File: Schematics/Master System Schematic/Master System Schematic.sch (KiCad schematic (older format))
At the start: 30 parts, among them J1 GND, J2 TS+, J3 TS-, SW1 GLVMS, SW2 SideMounted (BRB), SW3 SideMounted (BRB)

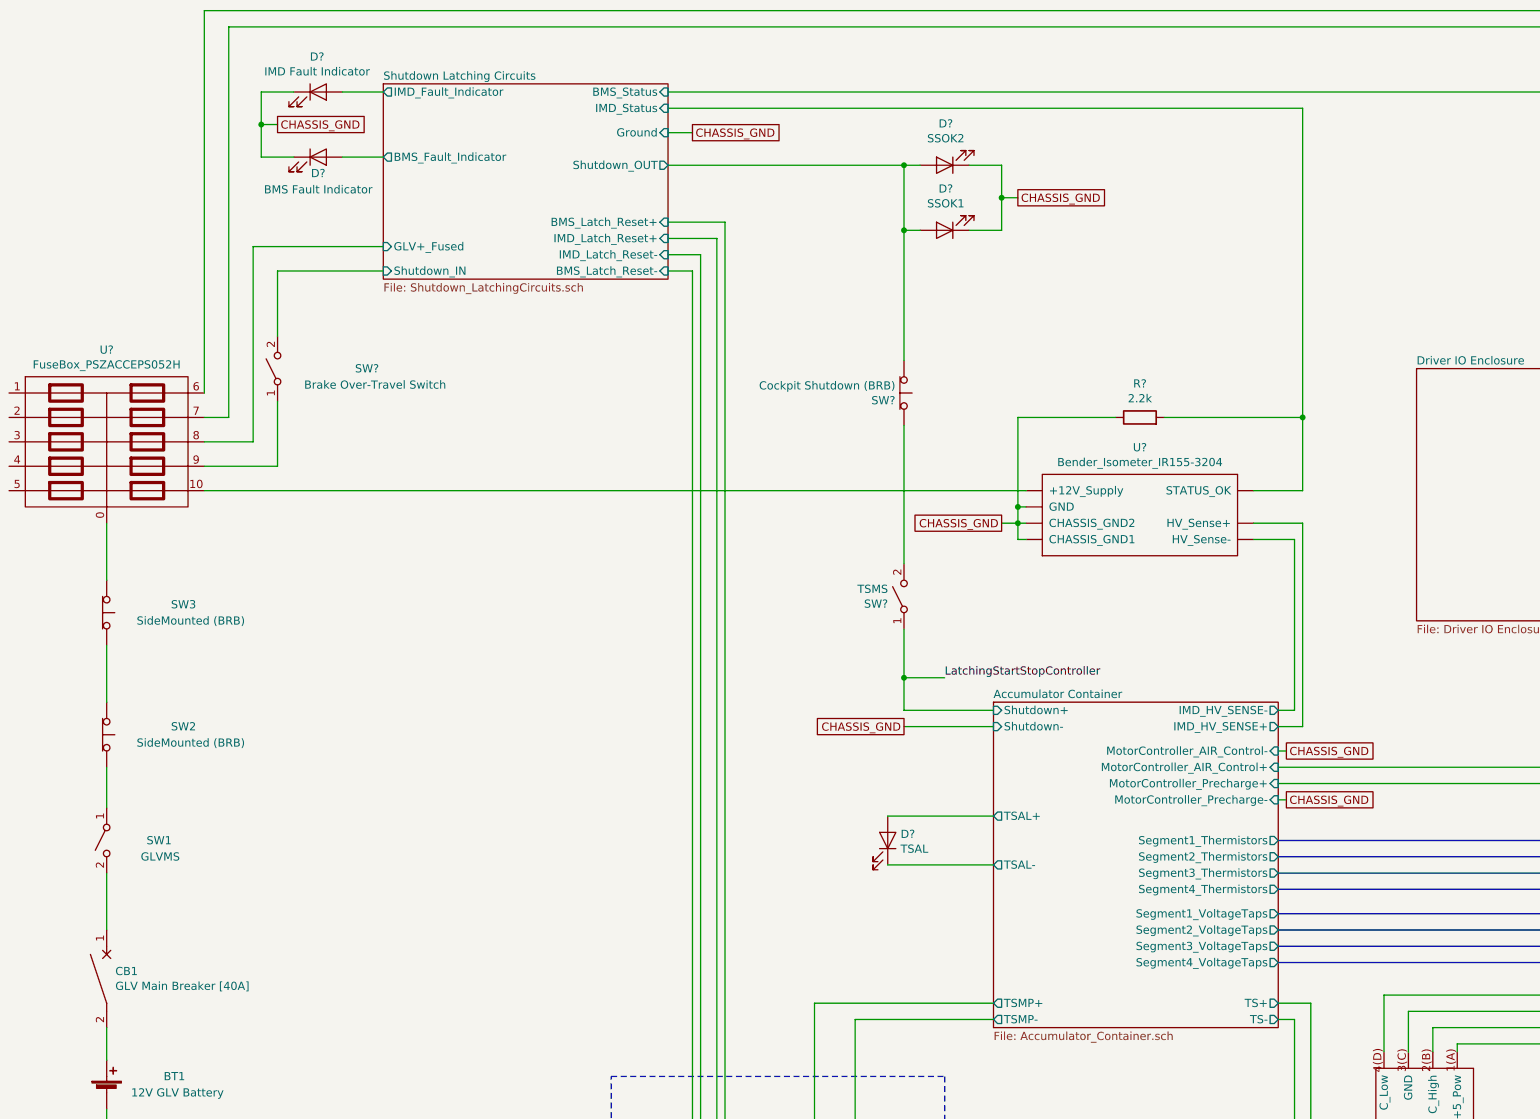
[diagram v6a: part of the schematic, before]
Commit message: Wire run updates, prettying up
>Moved SMDs and HVDs outside of accumulator container for consistency (all human activated switches and indicators should be in top level sheet)
>minor wire run updates and cleanup in accumulator container
>minor wire run cleanup in master schematic
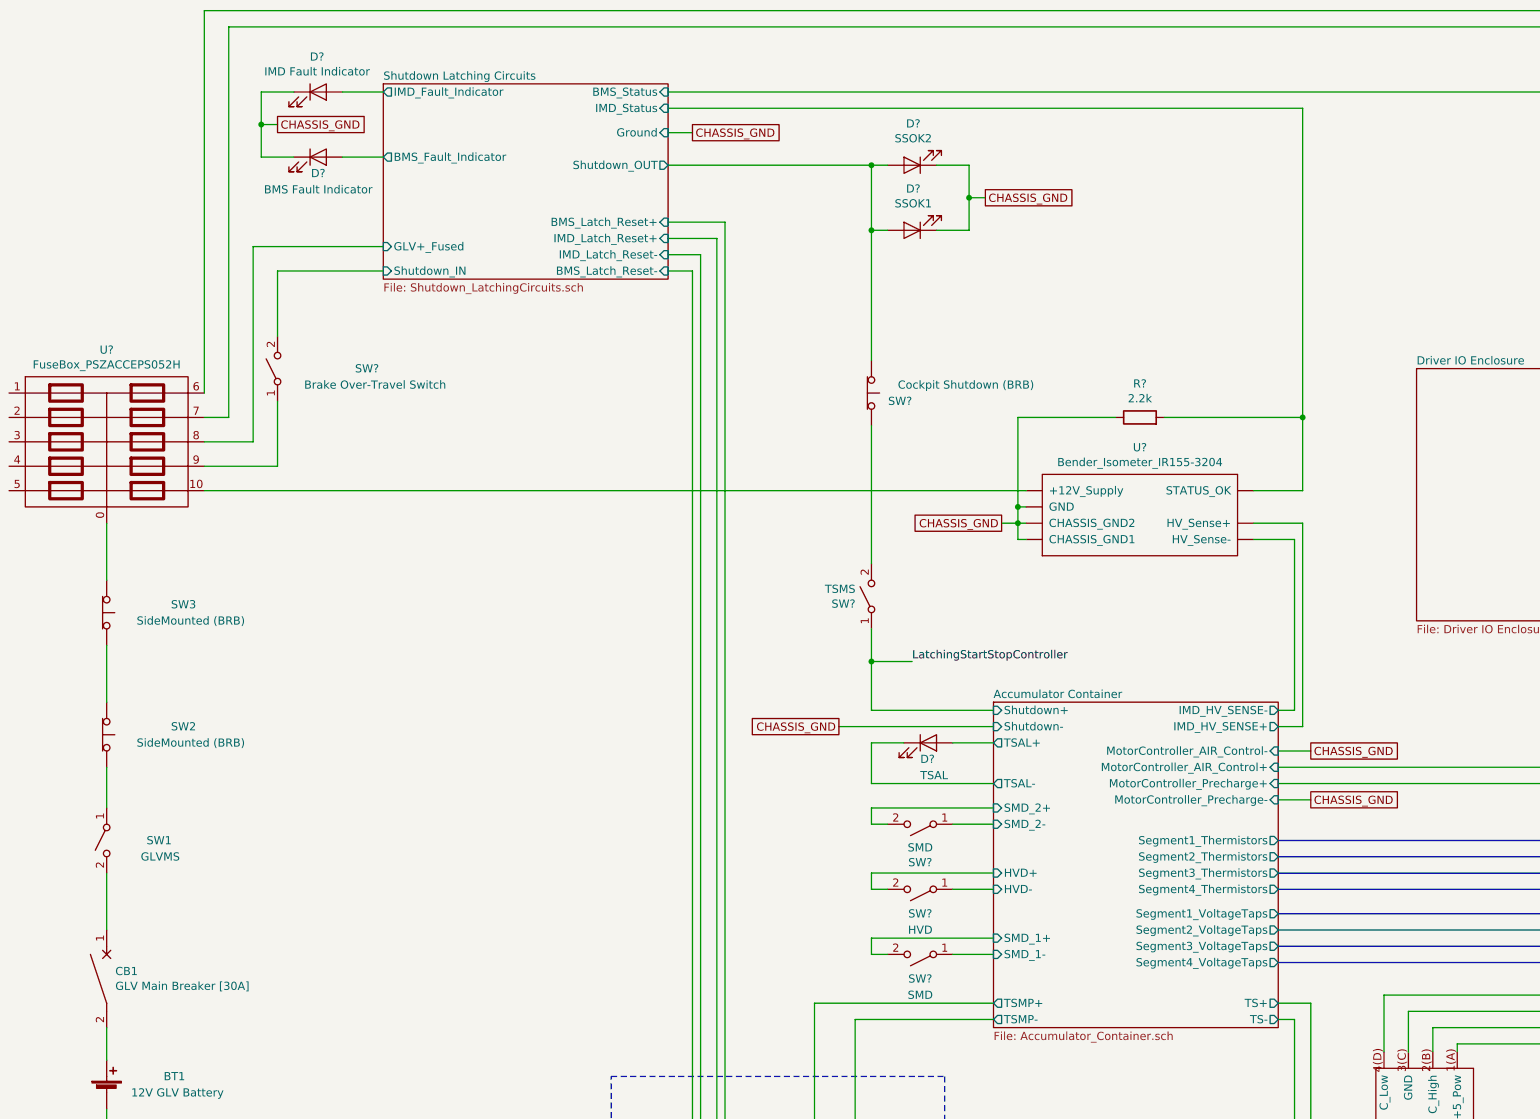
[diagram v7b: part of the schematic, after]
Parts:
- added SW?: HVD, symbol Switch:SW_SPST
- added SW? (x2): SMD, symbol Switch:SW_SPST
- CB1: value GLV Main Breaker [40A] -> GLV Main Breaker [30A]
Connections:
- new net: U?.23 (CANB_H), U?.6, U?.8 (Reverse_Enable_Switch)
- new net: U?.~ (AC3), U?.~ (TS-) (x2)
- new net Accumulator Container/HVD+: SW?.2 (B)
- new net Accumulator Container/HVD-: SW?.1 (A)
- new net Accumulator Container/SMD_1+: SW?.2 (B)
- new net Accumulator Container/SMD_1-: SW?.1 (A)
- new net Accumulator Container/SMD_2+: SW?.2 (B)
- new net Accumulator Container/SMD_2-: SW?.1 (A)
- now unconnected: U?.23 (CANB_H), U?.8 (Reverse_Enable_Switch)
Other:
- moved on the sheet: D?, SW?
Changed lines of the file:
@@
 L Switch:SW_Push_Open SW?
 U 1 1 5F67997D
-P 6150 3350
+P 5950 3350
 AR Path="/5F45AFB3/5F67997D" Ref="SW?"  Part="1"
 AR Path="/5F67997D" Ref="SW?"  Part="1"
-F 0 "SW?" V 6196 3297 50  0000 R CNN
-F 1 "Cockpit Shutdown (BRB)" V 6105 3297 50  0000 R CNN
-F 2 "" H 6150 3550 50  0001 C CNN
-F 3 "https://www.mouser.com/datasheet/2/307/a165e_ds_e_11_2_csm1264-1291086.pdf" H 6150 3550 50  0001 C CNN
-	1    6150 3350
+F 0 "SW?" V 6000 3600 50  0000 R CNN
+F 1 "Cockpit Shutdown (BRB)" V 5900 4350 50  0000 R CNN
+F 2 "" H 5950 3550 50  0001 C CNN
+F 3 "https://www.mouser.com/datasheet/2/307/a165e_ds_e_11_2_csm1264-1291086.pdf" H 5950 3550 50  0001 C CNN
+	1    5950 3350
 	0    1    1    0
 $EndComp
@@
 L Switch:SW_SPST SW?
 U 1 1 5F67998A
-P 6150 4600
+P 5950 4600
 AR Path="/5F45AFB3/5F67998A" Ref="SW?"  Part="1"
 AR Path="/5F67998A" Ref="SW?"  Part="1"
-F 0 "SW?" V 6104 4698 50  0000 L CNN
-F 1 "TSMS" V 6195 4698 50  0000 L CNN
-F 2 "" H 6150 4600 50  0001 C CNN
-F 3 "https://www.pegasusautoracing.com/pdfs/4430WiringInstructions.pdf" H 6150 4600 50  0001 C CNN
-	1    6150 4600
+F 0 "SW?" V 5904 4698 50  0000 L CNN
+F 1 "TSMS" V 5995 4698 50  0000 L CNN
+F 2 "" H 5950 4600 50  0001 C CNN
+F 3 "https://www.pegasusautoracing.com/pdfs/4430WiringInstructions.pdf" H 5950 4600 50  0001 C CNN
+	1    5950 4600
 	0    -1   -1   0
 $EndComp
 Text GLabel 1400 7900 2    50   UnSpc ~ 0
 CHASSIS_GND
-Text Label 6400 5100 0    50   ~ 0
+Text Label 6200 5000 0    50   ~ 0
 LatchingStartStopController
-Text GLabel 6850 2150 2    50   UnSpc ~ 0
-CHASSIS_GND
-Wire Wire Line
-	6750 2350 6750 2150
-Wire Wire Line
-	6550 1950 6750 1950
+Text GLabel 6650 2150 2    50   UnSpc ~ 0
+CHASSIS_GND
+Wire Wire Line
+	6550 2350 6550 2150
+Wire Wire Line
+	6350 1950 6550 1950
 $Comp
 L Device:LED D?
 U 1 1 5F67996F
-P 6400 2350
+P 6200 2350
 AR Path="/5F45AFB3/5F67996F" Ref="D?"  Part="1"
 AR Path="/5F67996F" Ref="D?"  Part="1"
-F 0 "D?" H 6393 2095 50  0000 C CNN
-F 1 "SSOK1" H 6393 2186 50  0000 C CNN
-F 2 "" H 6400 2350 50  0001 C CNN
-F 3 "https://www.superbrightleds.com/moreinfo/marker-clearance/rectangle-led-truck-and-trailer-lights-4-double-bullseye-led-side-clearance-lights-w-12-high-flux-leds-pigtail-connector/596/" H 6400 2350 50  0001 C CNN
-	1    6400 2350
+F 0 "D?" H 6193 2095 50  0000 C CNN
+F 1 "SSOK1" H 6193 2186 50  0000 C CNN
+F 2 "" H 6200 2350 50  0001 C CNN
+F 3 "https://www.superbrightleds.com/moreinfo/marker-clearance/rectangle-led-truck-and-trailer-lights-4-double-bullseye-led-side-clearance-lights-w-12-high-flux-leds-pigtail-connector/596/" H 6200 2350 50  0001 C CNN
+	1    6200 2350
 	-1   0    0    1
 $EndComp
@@
 L Device:LED D?
 U 1 1 5F679969
-P 6400 1950
+P 6200 1950
 AR Path="/5F45AFB3/5F679969" Ref="D?"  Part="1"
 AR Path="/5F679969" Ref="D?"  Part="1"
-F 0 "D?" H 6393 1695 50  0000 C CNN
-F 1 "SSOK2" H 6393 1786 50  0000 C CNN
-F 2 "" H 6400 1950 50  0001 C CNN
-F 3 "https://www.superbrightleds.com/moreinfo/marker-clearance/rectangle-led-truck-and-trailer-lights-4-double-bullseye-led-side-clearance-lights-w-12-high-flux-leds-pigtail-connector/596/" H 6400 1950 50  0001 C CNN
-	1    6400 1950
+F 0 "D?" H 6193 1695 50  0000 C CNN
+F 1 "SSOK2" H 6193 1786 50  0000 C CNN
+F 2 "" H 6200 1950 50  0001 C CNN
+F 3 "https://www.superbrightleds.com/moreinfo/marker-clearance/rectangle-led-truck-and-trailer-lights-4-double-bullseye-led-side-clearance-lights-w-12-high-flux-leds-pigtail-connector/596/" H 6200 1950 50  0001 C CNN
+	1    6200 1950
 	-1   0    0    1
 $EndComp
@@
 	1400 7900 1250 7900
 Wire Wire Line
-	6850 2150 6750 2150
-Connection ~ 6750 2150
-Wire Wire Line
-	6750 2150 6750 1950
+	6650 2150 6550 2150
+Connection ~ 6550 2150
+Wire Wire Line
+	6550 2150 6550 1950
 $Comp
 L Device:R R?
@@
 	1250 7750 1250 7900
 Wire Wire Line
-	6750 2350 6550 2350
+	6550 2350 6350 2350
 Wire Wire Line
 	1250 7250 1250 7450
@@
 	1250 4900 1250 5250
 Wire Wire Line
-	6400 5100 6150 5100
+	6200 5000 5950 5000
 $Comp
 L Connector:Conn_01x01_Female J3
@@
 Text Notes 4400 8900 0    50   ~ 0
 TSMP and Shutdown Reset Container
-Text GLabel 6150 5400 0    50   UnSpc ~ 0
+Text GLabel 5750 5400 0    50   UnSpc ~ 0
 CHASSIS_GND
 $Comp
@@
 F5 "TS-" O L 8850 9050 50
 $EndSheet
-Text GLabel 8500 5850 2    50   UnSpc ~ 0
+Text GLabel 8650 5850 2    50   UnSpc ~ 0
 CHASSIS_GND
 $Sheet
@@
 F4 "TS+" O R 8450 7100 50
 F5 "TS-" O R 8450 7200 50
-F6 "TSAL+" O L 6700 5950 50
-F7 "TSAL-" O L 6700 6250 50
+F6 "TSAL+" O L 6700 5500 50
+F7 "TSAL-" O L 6700 5750 50
 F8 "IMD_HV_SENSE-" O R 8450 5300 50
 F9 "IMD_HV_SENSE+" O R 8450 5400 50
@@
 F22 "MotorController_Precharge-" I R 8450 5850 50
 F23 "MotorController_Precharge+" I R 8450 5750 50
+F24 "HVD-" I L 6700 6400 50
+F25 "HVD+" I L 6700 6300 50
+F26 "SMD_2-" I L 6700 6000 50
+F27 "SMD_2+" I L 6700 5900 50
+F28 "SMD_1-" I L 6700 6800 50
+F29 "SMD_1+" I L 6700 6700 50
 $EndSheet
 Wire Wire Line
@@
 	8450 5400 8600 5400
 Wire Wire Line
-	6150 2350 6250 2350
+	5950 2350 6050 2350
 Wire Wire Line
 	8550 4250 8300 4250
@@
 	1850 1000 1850 3350
 Wire Wire Line
-	6150 5300 6700 5300
-Wire Wire Line
 	8450 7100 8650 7100
-Wire Wire Line
-	8500 5850 8450 5850
 $Comp
 L Device:CircuitBreaker_1P CB1
@@
 P 1250 6950
 F 0 "CB1" H 1303 6996 50  0000 L CNN
-F 1 "GLV Main Breaker [40A]" H 1303 6905 50  0000 L CNN
+F 1 "GLV Main Breaker [30A]" H 1303 6905 50  0000 L CNN
 F 2 "" H 1250 6950 50  0001 C CNN
 F 3 "~" H 1250 6950 50  0001 C CNN
@@
 $EndComp
 Wire Wire Line
-	6150 1950 6150 2350
-Connection ~ 6150 1950
-Wire Wire Line
-	6150 1950 6250 1950
-Wire Wire Line
-	6150 2350 6150 3150
-Connection ~ 6150 2350
-Wire Wire Line
-	6150 4400 6150 3550
+	5950 1950 5950 2350
+Wire Wire Line
+	5950 1950 6050 1950
+Wire Wire Line
+	5950 2350 5950 3150
+Connection ~ 5950 2350
+Wire Wire Line
+	5950 4400 5950 3550
 Wire Notes Line
 	4350 8750 4350 7550
@@
 L Device:LED D?
 U 1 1 5FA58D8C
-P 6050 6100
-F 0 "D?" V 6089 6179 50  0000 L CNN
-F 1 "TSAL" V 5998 6179 50  0000 L CNN
-F 2 "" H 6050 6100 50  0001 C CNN
-F 3 "~" H 6050 6100 50  0001 C CNN
-	1    6050 6100
-	0    1    -1   0
-$EndComp
-Wire Wire Line
-	6700 5950 6050 5950
-Wire Wire Line
-	6700 6250 6050 6250
+P 6300 5500
+F 0 "D?" H 6250 5400 50  0000 L CNN
+F 1 "TSAL" H 6250 5300 50  0000 L CNN
+F 2 "" H 6300 5500 50  0001 C CNN
+F 3 "~" H 6300 5500 50  0001 C CNN
+	1    6300 5500
+	1    0    0    -1
+$EndComp
 Wire Wire Line
 	15300 5750 15300 7700
@@
 $EndComp
 Wire Wire Line
-	4700 1950 6150 1950
-Wire Wire Line
 	4700 1600 8600 1600
 Wire Wire Line
@@
 Wire Wire Line
 	2300 2600 2300 3000
-Connection ~ 6150 5100
 Text GLabel 4850 1750 2    50   UnSpc ~ 0
 CHASSIS_GND
@@
 Wire Wire Line
 	1850 3950 6900 3950
-Wire Wire Line
-	6150 5100 6150 5300
 $Comp
 L Switch:SW_SPST_Temperature SW?
@@
 	12750 4250 12950 4250
 Wire Wire Line
-	6150 4800 6150 5100
+	5950 4800 5950 5000
 Wire Wire Line
 	8600 5400 8600 4150
 Wire Wire Line
 	8550 4250 8550 5300
-Text GLabel 8500 5550 2    50   UnSpc ~ 0
-CHASSIS_GND
-Wire Wire Line
-	8500 5550 8450 5550
+Text GLabel 8650 5550 2    50   UnSpc ~ 0
+CHASSIS_GND
 Wire Wire Line
 	8450 5650 15400 5650
@@
 Wire Wire Line
 	15400 7950 15200 7950
-Wire Wire Line
-	6150 5400 6700 5400
+$Comp
+L Switch:SW_SPST SW?
+U 1 1 60DA2E32
+P 6250 6400
+AR Path="/5F45B05E/60DA2E32" Ref="SW?"  Part="1"
+AR Path="/60DA2E32" Ref="SW?"  Part="1"
+F 0 "SW?" H 6250 6550 50  0000 C CNN
+F 1 "HVD" H 6250 6650 50  0000 C CNN
+F 2 "" H 6250 6400 50  0001 C CNN
+F 3 "~" H 6250 6400 50  0001 C CNN
+	1    6250 6400
+	-1   0    0    1
+$EndComp
+$Comp
+L Switch:SW_SPST SW?
+U 1 1 60DA2E38
+P 6250 6000
+AR Path="/5F45B05E/60DA2E38" Ref="SW?"  Part="1"
+AR Path="/60DA2E38" Ref="SW?"  Part="1"
+F 0 "SW?" H 6250 6235 50  0000 C CNN
+F 1 "SMD" H 6250 6144 50  0000 C CNN
+F 2 "" H 6250 6000 50  0001 C CNN
+F 3 "~" H 6250 6000 50  0001 C CNN
+	1    6250 6000
+	-1   0    0    1
+$EndComp
+$Comp
+L Switch:SW_SPST SW?
+U 1 1 60DA2E3E
+P 6250 6800
+AR Path="/5F45B05E/60DA2E3E" Ref="SW?"  Part="1"
+AR Path="/60DA2E3E" Ref="SW?"  Part="1"
+F 0 "SW?" H 6250 6950 50  0000 C CNN
+F 1 "SMD" H 6250 7050 50  0000 C CNN
+F 2 "" H 6250 6800 50  0001 C CNN
+F 3 "~" H 6250 6800 50  0001 C CNN
+	1    6250 6800
+	-1   0    0    1
+$EndComp
+Wire Wire Line
+	6700 6000 6450 6000
+Wire Wire Line
+	6050 6000 5950 6000
+Wire Wire Line
+	5950 6000 5950 5900
+Wire Wire Line
+	5950 5900 6700 5900
+Wire Wire Line
+	6700 6400 6450 6400
+Wire Wire Line
+	6050 6400 5950 6400
+Wire Wire Line
+	5950 6400 5950 6300
+Wire Wire Line
+	5950 6300 6700 6300
+Wire Wire Line
+	6700 6800 6450 6800
+Wire Wire Line
+	6050 6800 5950 6800
+Wire Wire Line
+	5950 6800 5950 6700
+Wire Wire Line
+	5950 6700 6700 6700
+Wire Wire Line
+	6150 5500 5950 5500
+Wire Wire Line
+	5950 5500 5950 5750
+Wire Wire Line
+	6450 5500 6700 5500
+Wire Wire Line
+	5950 5750 6700 5750
+Wire Wire Line
+	5750 5400 6700 5400
+Wire Wire Line
+	8450 5550 8650 5550
+Wire Wire Line
+	8450 5850 8650 5850
+Wire Wire Line
+	5950 1950 4700 1950
+Connection ~ 5950 1950
+Connection ~ 5950 5000
+Wire Wire Line
+	5950 5000 5950 5300
+Wire Wire Line
+	5950 5300 6700 5300
 $EndSCHEMATC
